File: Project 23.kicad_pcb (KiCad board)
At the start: 2 copper layers, 62 x 42 mm, 65 parts, among them J11 SRX 1, J12 SRX 2, J13 SWD, J21 BATT +, J22 BATT-, J61 USB_Micro, J71 Micro_SD_Card_Det, SW11 UI_Btn, SW12 PWR_BTN, U1 STM32F103C8T7, U2 74AHCT1G125, U21 MCP73832, U31 NCP551, U32 MIC5504, U41 TPS6122x, U5 oled, Y11 8 MHz

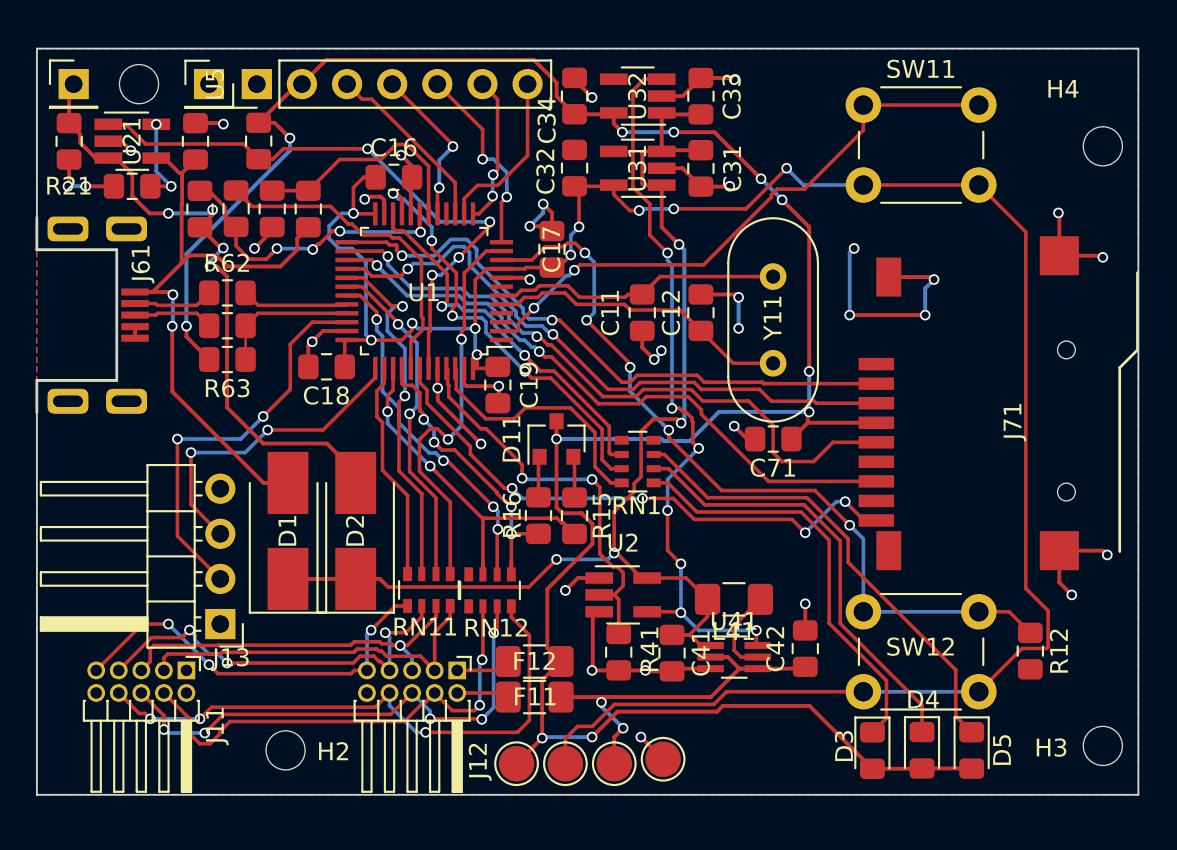
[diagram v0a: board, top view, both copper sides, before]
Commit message: 4 Layer with reworked layout
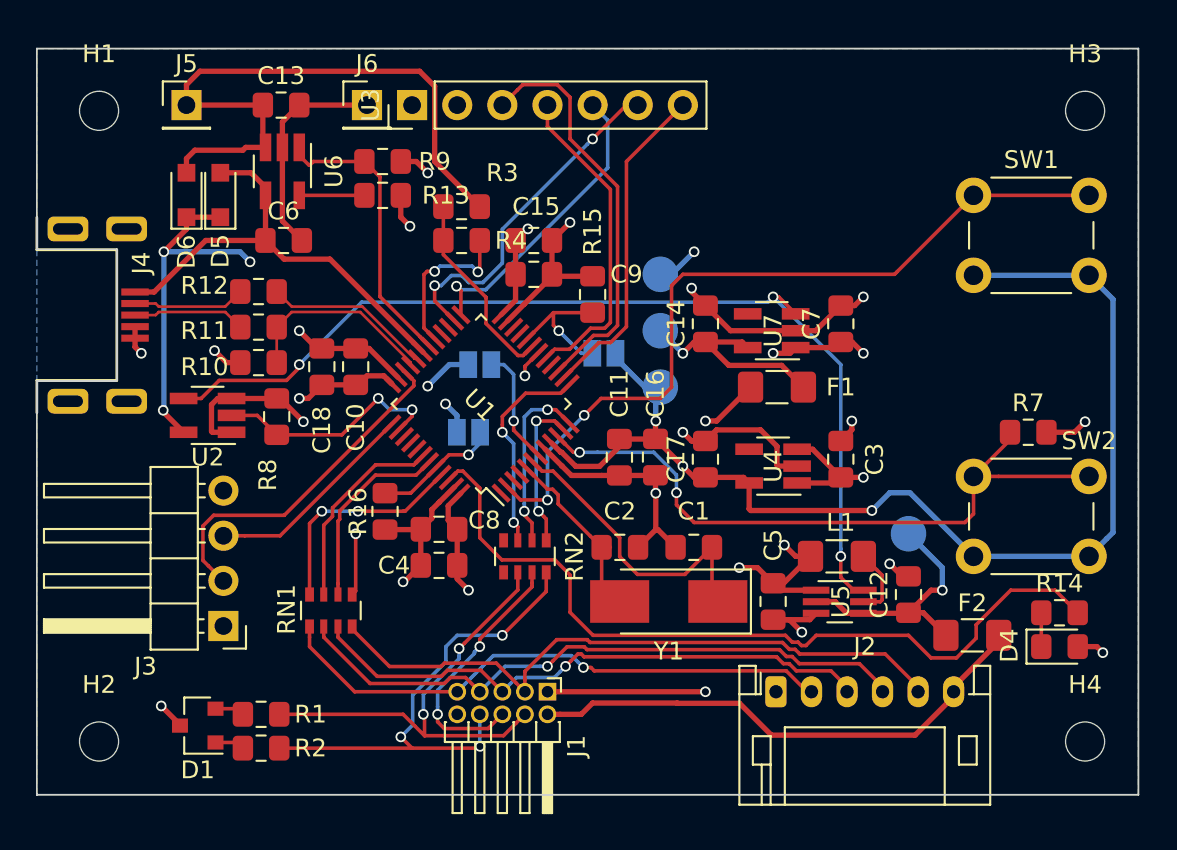
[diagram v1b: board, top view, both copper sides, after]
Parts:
- removed C19: 0.1uF, Capacitor_SMD:C_0805_2012Metric_Pad1.15x1.40mm_HandSolder
- removed C21, C22, C31, C32, C33, C34, C71: 1uF, Capacitor_SMD:C_0805_2012Metric_Pad1.15x1.40mm_HandSolder
- removed C41, C42: 10uF, Capacitor_SMD:C_0805_2012Metric_Pad1.15x1.40mm_HandSolder
- removed D11: MMBD1205, Package_TO_SOT_SMD:SOT-23
- removed D2: MBRS140, Diode_SMD:D_SMB_Handsoldering
- removed D3: LED, LED_SMD:LED_0805_2012Metric_Pad1.15x1.40mm_HandSolder
- removed F11, F12: 50mA, Fuse:Fuse_1206_3216Metric_Pad1.42x1.75mm_HandSolder
- removed J11: SRX 1, Connector_PinHeader_1.27mm:PinHeader_2x05_P1.27mm_Horizontal
- removed J12: SRX 2, Connector_PinHeader_1.27mm:PinHeader_2x05_P1.27mm_Horizontal
- removed J13: SWD, Connector_PinHeader_2.54mm:PinHeader_1x04_P2.54mm_Horizontal
- removed J21: BATT +, Connector_PinHeader_2.54mm:PinHeader_1x01_P2.54mm_Vertical
- removed J22: BATT-, Connector_PinHeader_2.54mm:PinHeader_1x01_P2.54mm_Vertical
- removed J71: Micro_SD_Card_Det, Project 23:micro sd holder
- removed L41: 4.7uH, Inductor_SMD:L_1206_3216Metric_Pad1.42x1.75mm_HandSolder
- removed R21: 5K1, Resistor_SMD:R_0805_2012Metric_Pad1.15x1.40mm_HandSolder
- removed R22, R41, R81, R82, R83, R84: 10k, Resistor_SMD:R_0805_2012Metric_Pad1.15x1.40mm_HandSolder
- removed R61, R62: 20R, Resistor_SMD:R_0805_2012Metric_Pad1.15x1.40mm_HandSolder
- removed R63: 1.5k, Resistor_SMD:R_0805_2012Metric_Pad1.15x1.40mm_HandSolder
- removed RN11, RN12: 1k, Resistor_SMD:R_Array_Convex_4x0603
- removed SW11: UI_Btn, Button_Switch_THT:SW_PUSH_6mm_H5mm
- removed SW12: PWR_BTN, Button_Switch_THT:SW_PUSH_6mm_H5mm
- removed TP31: 3V3SB, TestPoint:TestPoint_Pad_D2.0mm
- removed TP32: 3V3, TestPoint:TestPoint_Pad_D2.0mm
- removed TP41: 5V, TestPoint:TestPoint_Pad_D2.0mm
- removed TP75: GND, TestPoint:TestPoint_Pad_D2.0mm
- removed U21: MCP73832, Package_TO_SOT_SMD:SOT-23-5_HandSoldering
- removed U31: NCP551, Package_TO_SOT_SMD:SOT-23-5_HandSoldering
- removed U32: MIC5504, Package_TO_SOT_SMD:SOT-23-5_HandSoldering
- removed U41: TPS6122x, Package_TO_SOT_SMD:SOT-363_SC-70-6_Handsoldering
- removed Y11: 8 MHz, Crystal:Crystal_HC49-4H_Vertical
- added C1: 20p, Capacitor_SMD:C_0805_2012Metric_Pad1.15x1.40mm_HandSolder, F.Cu at (87.0, 68.1)
- added C10: 10n, Capacitor_SMD:C_0805_2012Metric_Pad1.15x1.40mm_HandSolder, F.Cu at (67.9, 57.9)
- added C13: 1uF, Capacitor_SMD:C_0805_2012Metric_Pad1.15x1.40mm_HandSolder, F.Cu at (63.7, 43.2)
- added C14: 1uF, Capacitor_SMD:C_0805_2012Metric_Pad1.15x1.40mm_HandSolder, F.Cu at (87.6, 55.5)
- added C15: 1u, Capacitor_SMD:C_0805_2012Metric_Pad1.15x1.40mm_HandSolder, F.Cu at (78.0, 50.8)
- added C2: 20p, Capacitor_SMD:C_0805_2012Metric_Pad1.15x1.40mm_HandSolder, F.Cu at (82.8, 68.1)
- added C3: 1uF, Capacitor_SMD:C_0805_2012Metric_Pad1.15x1.40mm_HandSolder, F.Cu at (95.2, 63.1)
- added C4: 1uF, Capacitor_SMD:C_0805_2012Metric_Pad1.15x1.40mm_HandSolder, F.Cu at (72.6, 69.1)
- added C5: 10uF, Capacitor_SMD:C_0805_2012Metric_Pad1.15x1.40mm_HandSolder, F.Cu at (91.4, 71.1)
- added C6: 1uF, Capacitor_SMD:C_0805_2012Metric_Pad1.15x1.40mm_HandSolder, F.Cu at (63.9, 50.8)
- added C7: 1uF, Capacitor_SMD:C_0805_2012Metric_Pad1.15x1.40mm_HandSolder, F.Cu at (95.2, 55.5)
- added C8: 10n, Capacitor_SMD:C_0805_2012Metric_Pad1.15x1.40mm_HandSolder, F.Cu at (72.6, 67.1)
- added C9: 10n, Capacitor_SMD:C_0805_2012Metric_Pad1.15x1.40mm_HandSolder, F.Cu at (78.0, 52.7)
- added D6: CU10S30, Diode_SMD:D_SOD-323_HandSoldering, F.Cu at (58.4, 48.2)
- added F1: 100mA, Fuse:Fuse_1206_3216Metric_Pad1.42x1.75mm_HandSolder, F.Cu at (91.7, 59.1)
- added F2: 100mA, Fuse:Fuse_1206_3216Metric_Pad1.42x1.75mm_HandSolder, F.Cu at (102.7, 73.0)
- added J1: SRX 2, Connector_PinHeader_1.27mm:PinHeader_2x05_P1.27mm_Horizontal, F.Cu at (78.7, 76.2)
- added J2: SPARK Encoder Port, Connector_JST:JST_PH_S6B-PH-K_1x06_P2.00mm_Horizontal, F.Cu at (91.6, 76.2)
- added J3: SWD, Connector_PinHeader_2.54mm:PinHeader_1x04_P2.54mm_Horizontal, F.Cu at (60.5, 72.5)
- added J5: BATT +, Connector_PinHeader_2.54mm:PinHeader_1x01_P2.54mm_Vertical, F.Cu at (58.4, 43.2)
- added J6: BATT-, Connector_PinHeader_2.54mm:PinHeader_1x01_P2.54mm_Vertical, F.Cu at (68.6, 43.2)
- added JP1: BOOT1, Jumper:SolderJumper-2_P1.3mm_Open_Pad1.0x1.5mm, B.Cu at (81.9, 57.1)
- added JP2: Reset, Jumper:SolderJumper-2_P1.3mm_Open_Pad1.0x1.5mm, B.Cu at (74.9, 57.8)
- added JP3: BOOT0, Jumper:SolderJumper-2_P1.3mm_Open_Pad1.0x1.5mm, B.Cu at (74.3, 61.6)
- added L1: 4.7uH, Inductor_SMD:L_1206_3216Metric_Pad1.42x1.75mm_HandSolder, F.Cu at (95.0, 68.6)
- added R1: 10k, Resistor_SMD:R_0805_2012Metric_Pad1.15x1.40mm_HandSolder, F.Cu at (62.6, 77.5)
- added R10: 1.5k, Resistor_SMD:R_0805_2012Metric_Pad1.15x1.40mm_HandSolder, F.Cu at (62.5, 57.7)
- added R11: 20R, Resistor_SMD:R_0805_2012Metric_Pad1.15x1.40mm_HandSolder, F.Cu at (62.5, 55.7)
- added R13: 5K1, Resistor_SMD:R_0805_2012Metric_Pad1.15x1.40mm_HandSolder, F.Cu at (69.5, 48.3)
- added R14: 1.5k, Resistor_SMD:R_0805_2012Metric_Pad1.15x1.40mm_HandSolder, F.Cu at (107.6, 71.8)
- added R2: 10k, Resistor_SMD:R_0805_2012Metric_Pad1.15x1.40mm_HandSolder, F.Cu at (62.6, 79.4)
- added R3: 10k, Resistor_SMD:R_0805_2012Metric_Pad1.15x1.40mm_HandSolder, F.Cu at (73.9, 48.9)
- added R4: 10k, Resistor_SMD:R_0805_2012Metric_Pad1.15x1.40mm_HandSolder, F.Cu at (73.9, 50.8)
- added R7: 10k, Resistor_SMD:R_0805_2012Metric_Pad1.15x1.40mm_HandSolder, F.Cu at (105.8, 61.6)
- added R8: 10k, Resistor_SMD:R_0805_2012Metric_Pad1.15x1.40mm_HandSolder, F.Cu at (63.5, 60.7)
- added R9: 10k, Resistor_SMD:R_0805_2012Metric_Pad1.15x1.40mm_HandSolder, F.Cu at (69.5, 46.4)
- added RN2: 1k, Resistor_SMD:R_Array_Convex_4x0603, F.Cu at (77.5, 68.6)
- added SW1: UI_Btn, Button_Switch_THT:SW_PUSH_6mm_H5mm, F.Cu at (102.7, 48.3)
- added SW2: PWR_BTN, Button_Switch_THT:SW_PUSH_6mm_H5mm, F.Cu at (102.7, 64.1)
- added TP1: GND, TestPoint:TestPoint_Pad_D2.0mm, B.Cu at (85.1, 52.7)
- added TP2: 3V3SB, TestPoint:TestPoint_Pad_D2.0mm, B.Cu at (85.1, 59.1)
- added TP3: 5V, TestPoint:TestPoint_Pad_D2.0mm, B.Cu at (99.1, 67.3)
- added TP4: 3V3, TestPoint:TestPoint_Pad_D2.0mm, B.Cu at (85.1, 55.9)
- added U3: oled, Connector_PinHeader_2.54mm:PinHeader_1x07_P2.54mm_Vertical, F.Cu at (71.1, 43.2)
- added U4: NCP551, Package_TO_SOT_SMD:SOT-23-5_HandSoldering, F.Cu at (91.4, 63.5)
- added U6: MCP73832, Package_TO_SOT_SMD:SOT-23-5_HandSoldering, F.Cu at (63.8, 46.9)
- added U7: MIC5504, Package_TO_SOT_SMD:SOT-23-5_HandSoldering, F.Cu at (91.4, 55.9)
- added Y1: 8 MHz, Crystal:Crystal_SMD_Abracon_ABM3-2Pin_5.0x3.2mm_HandSoldering, F.Cu at (85.6, 71.1)
- C11: value 20p -> 10n
- C12: value 20p -> 10uF
- C16, C17, C18: value 0.1uF -> 1u
- D1: value MBRS140 -> MMBD1205; footprint Diode_SMD:D_SMB_Handsoldering -> Package_TO_SOT_SMD:SOT-23
- D5: value LED -> CU10S30; footprint LED_SMD:LED_0805_2012Metric_Pad1.15x1.40mm_HandSolder -> Diode_SMD:D_SOD-323_HandSoldering
- R12: value 10k -> 20R
- U2: value 74AHCT1G125 -> 74AHC1G125
- U5: value oled -> TPS6122x; footprint Connector_PinHeader_2.54mm:PinHeader_1x07_P2.54mm_Vertical -> Package_TO_SOT_SMD:SOT-363_SC-70-6_Handsoldering
- moved D5 52.6 mm to (60.3, 48.2), turned to 90 degrees
- moved R12 47.9 mm to (62.5, 53.7), turned to 0 degrees
- moved U5 43.9 mm to (95.2, 71.1), turned to 0 degrees
- moved H3 35.8 mm to (109.0, 43.5)
- moved H4 33.5 mm to (109.0, 79.0)
- moved U2 25.5 mm to (59.6, 60.6), turned to 180 degrees
- moved C16 21.6 mm to (84.8, 63.0), turned to 270 degrees
- moved C12 19.7 mm to (99.1, 70.7)
- moved RN1 19.2 mm to (66.5, 71.6), turned to 270 degrees
- moved C17 14.6 mm to (87.6, 63.1)
- moved R15 12.5 mm to (81.3, 53.8)
- moved D1 12.1 mm to (59.1, 78.1), turned to 180 degrees
- moved H2 10.5 mm to (53.5, 79.0)
- moved D4 9.69 mm to (107.6, 73.7), turned to 0 degrees
- moved R16 8.64 mm to (69.6, 66.0)
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- renumbered J61 to J4
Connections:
- C11 pad 1: Net-(C11-Pad1) -> /3V3SB
- C12 pad 1: Net-(C12-Pad1) -> +5V
- D1 pad 1: VCC -> Net-(D1-Pad1)
- D1 pad 2: VBUS -> Net-(D1-Pad2)
- D5 pad 1: Net-(D5-Pad1) -> VCC
- D5 pad 2: +3V3 -> VBUS
- R12 pad 1: /Power_Btn -> /P-
- R12 pad 2: GND -> /D-
- R15 pad 1: Net-(D11-Pad2) -> GND
- R15 pad 2: /Fwd_Limit -> Net-(JP1-Pad1)
- R16 pad 1: Net-(D11-Pad1) -> Net-(JP3-Pad2)
- R16 pad 2: /Rev_Limit -> GND
- RN1 pad 1: (no net) -> /Ana_In
- RN1 pad 2: /Pwr_LED -> /Quad_B
- RN1 pad 3: /Rev_LED -> /Quad_A
- RN1 pad 4: /Fwd_LED -> /Quad_Index
- RN1 pad 6: Net-(D4-Pad1) -> Net-(J1-Pad7)
- RN1 pad 7: Net-(D5-Pad1) -> Net-(J1-Pad5)
- RN1 pad 8: (no net) -> Net-(J1-Pad3)
- U1 pad 11: /Ana_In -> /Rev_Limit
- U1 pad 12: /OLED_RES -> /Trigger
- U1 pad 13: /OLED_DC -> /Fwd_Limit
- U1 pad 18: /VBus_Mon -> /Ana_In
- U1 pad 20: GND -> Net-(JP1-Pad1)
- U1 pad 21: /Rev_LED -> (no net)
- U1 pad 22: /Pwr_LED -> (no net)
- U1 pad 25: /SS2 -> /OLED_RES
- U1 pad 26: /SCK2 -> /OLED_DC
- U1 pad 27: /MISO2 -> (no net)
- U1 pad 28: /MOSI2 -> (no net)
- U1 pad 29: /Quad_A -> /R_DIV_En
- U1 pad 30: /Quad_B -> /Stat
- U1 pad 31: /Trigger -> VBUS
- U1 pad 38: /Quad_Index -> /PWR_EN_3V
- U1 pad 39: /Fwd_Limit -> (no net)
- U1 pad 40: /Rev_Limit -> (no net)
- U1 pad 41: /R_DIV_En -> (no net)
- U1 pad 42: /SD_CD -> /Quad_A
- U1 pad 43: /Stat -> /Quad_B
- U1 pad 44: GND -> Net-(JP3-Pad2)
- U1 pad 45: Net-(R41-Pad2) -> /Quad_Index
- U1 pad 46: /Fwd_LED -> /Pwr_LED
- U1 pad 5: Net-(C12-Pad1) -> Net-(C2-Pad1)
- U1 pad 6: Net-(C11-Pad1) -> Net-(C1-Pad1)
- U1 pad 7: (no net) -> /Reset
- U2 pad 2: Net-(R41-Pad2) -> /PWR_EN_3V
- U5 pad 1: GND -> VCC
- U5 pad 2: +3V3 -> +5V
- U5 pad 3: /SCK -> GND
- U5 pad 4: /MOSI -> +5V
- U5 pad 5: /OLED_RES -> Net-(L1-Pad1)
- U5 pad 6: /OLED_DC -> /PWR_EN
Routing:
- net +3V3: track 135.4 -> 19.0 mm, vias 11 -> 5
- net /3V3SB: track 123.3 -> 86.2 mm, vias 10 -> 7
- net Net-(J1-Pad3): track 0.00 -> 36.9 mm
- net /SCK2: track 36.8 -> 0.00 mm, vias 2 -> 0
- net Net-(J1-Pad7): track 0.00 -> 35.9 mm, vias 0 -> 1
- net /MISO2: track 35.6 -> 0.00 mm, vias 2 -> 0
- net /MOSI2: track 35.2 -> 0.00 mm, vias 2 -> 0
- net /SS2: track 34.9 -> 0.00 mm, vias 2 -> 0
- net Net-(J11-Pad8): track 32.8 -> 0.00 mm, vias 3 -> 0
- net Net-(J1-Pad5): track 0.00 -> 32.7 mm, vias 0 -> 1
- net /SD_CD: track 31.9 -> 0.00 mm, vias 4 -> 0
- net Net-(F2-Pad2): track 0.00 -> 29.3 mm
- net Net-(J11-Pad6): track 29.1 -> 0.00 mm, vias 5 -> 0
- net Net-(J1-Pad8): track 0.00 -> 28.2 mm, vias 0 -> 3
- net Net-(F1-Pad1): track 0.00 -> 27.5 mm, vias 0 -> 2
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- added copper zone on In2.Cu, net +3V3
- added copper zone on In2.Cu, net /3V3SB
- added copper zone on In1.Cu, net GND
- removed copper zone on F.Cu, net GND
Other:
- copper layers 2 -> 4
- net class Power: trace_width 0.22 -> 0.3
- board text removed: "Goldfish Electronics"
- board text removed: "Project 23 HW v0.7"

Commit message: Added logo and rearraged silkscreen
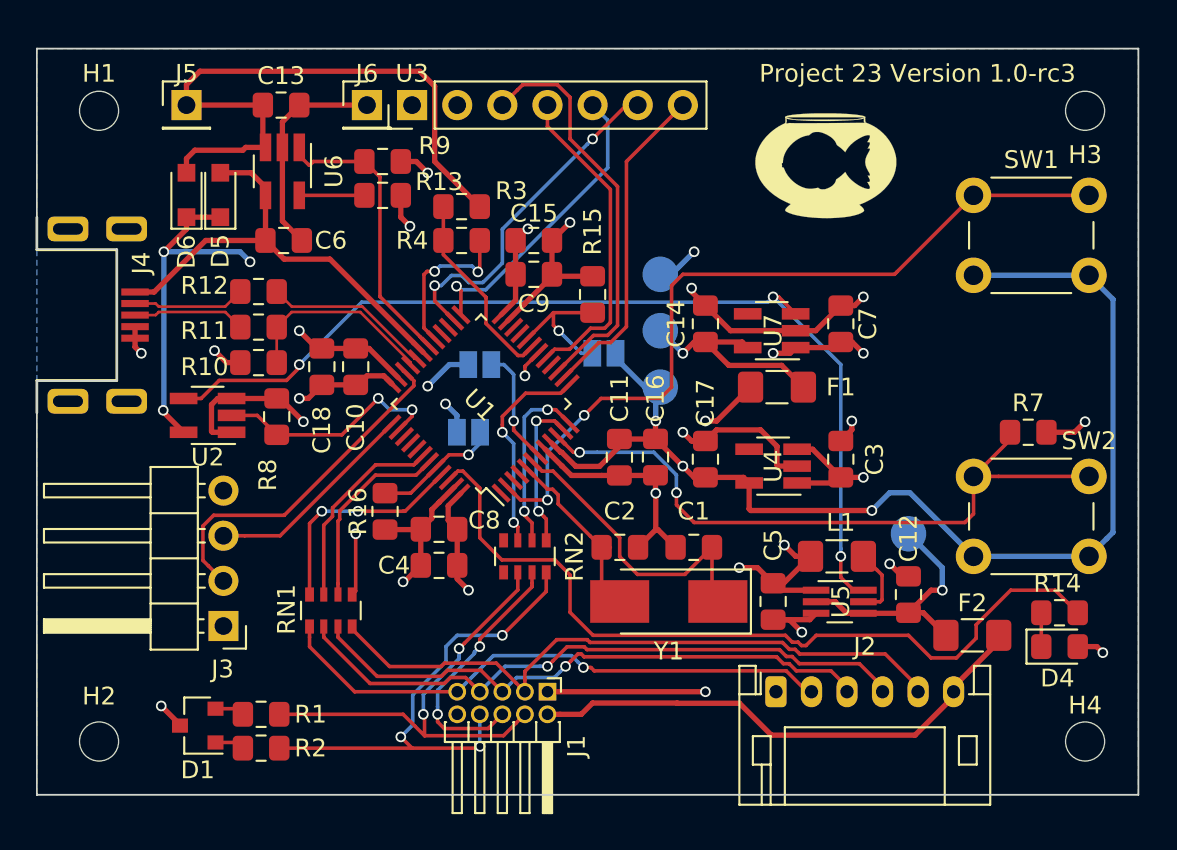
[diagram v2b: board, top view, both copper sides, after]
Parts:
- added H5: Logo, Project 23:goldfish, F.Cu at (94.5, 46.7)
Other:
- board text added: "Project 23 Version 1.0-rc3"
